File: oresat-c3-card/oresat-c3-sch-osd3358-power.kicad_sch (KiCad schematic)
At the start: 36 parts, among them Q6 MMBT2907, U1 OSD3358-1G-ISM, U10 SN74AUC1G07DCKR, U14 TLVH431

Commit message: Design review on power and RF
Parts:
- U1: Distributor (none) -> DigiKey; MPN OSD3358-1G-ISM -> OSD3358-512M-BSM
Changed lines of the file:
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@@
 			)
 		)
+		(property "Sim.Pins" "1=K 2=A"
+			(at 298.45 82.55 0)
+			(effects
+				(font
+					(size 1.27 1.27)
+				)
+				(hide yes)
+			)
+		)
 		(pin "1"
 		)
@@
 			)
 		)
-		(property "Description" "Embedded Module ARM® Cortex®-A8, AM3358 1GHz 1GB"
+		(property "Description" "OSD335x Embedded Module 1GHz 512MB"
 			(at 224.79 132.08 0)
 			(effects
@@
 			)
 		)
-		(property "MPN" "OSD3358-1G-ISM"
+		(property "MPN" "OSD3358-512M-BSM"
 			(at 224.79 132.08 0)
 			(effects
@@
 			)
 		)
+		(property "Distributor" "DigiKey"
+			(at 224.79 30.48 0)
+			(effects
+				(font
+					(size 1.27 1.27)
+				)
+				(hide yes)
+			)
+		)
 		(pin "C10"
 		)
@@
 			)
 		)
-		(property "Description" "Bipolar (BJT) Transistor PNP 60 V 600 mA 200MHz 250 mW Surface Mount TO-236AB"
+		(property "Description" "PNP transistor, base/emitter/collector"
 			(at 288.29 132.08 0)
 			(effects
@@
 			(at 288.29 132.08 0)
 			(effects
+				(font
+					(size 1.27 1.27)
+				)
+				(hide yes)
+			)
+		)
+		(property "Sim.Device" "PNP"
+			(at 288.29 132.08 0)
+			(effects
+				(font
+					(size 1.27 1.27)
+				)
+				(hide yes)
+			)
+		)
+		(property "Sim.Pins" "1=B 2=E 3=C"
+			(at 288.29 132.08 0)
+			(effects

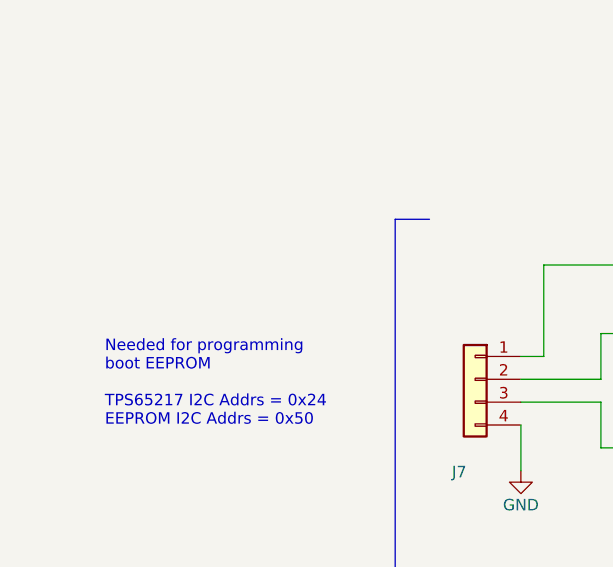
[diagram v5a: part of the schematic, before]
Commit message: Design review on C3 v7.0
Glenn and Andrew did a design review. Removed fiducials on back of board. Lots of schematic fixes, including
direction connection of TCXOs to AT86s, corrected LPF of CLKO from AT86 to the synth reference, fixed drive
levels both QPC switches in UHF radio, confirmed QPC directions, and some minor polishing.
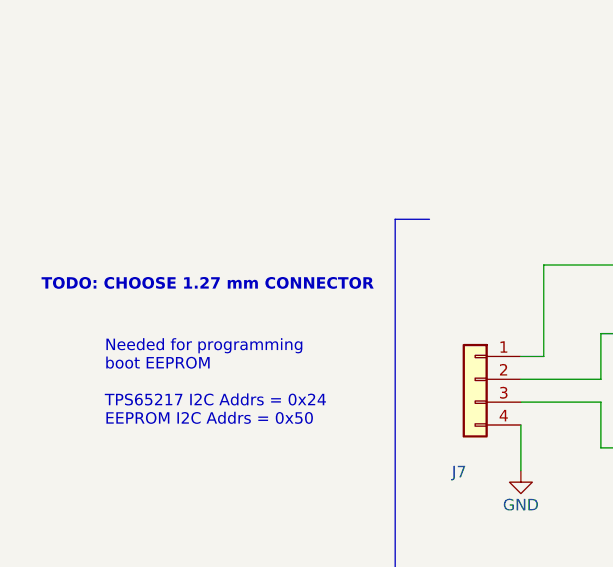
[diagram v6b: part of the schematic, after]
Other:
- note added: "TODO: CHOOSE 1.27 mm CONNECTOR"
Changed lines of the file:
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@@
+		)
+	)
+	(text "TODO: CHOOSE 1.27 mm CONNECTOR"
+		(exclude_from_sim no)
+		(at 130.302 187.706 0)
+		(effects
+			(font
+				(size 1.27 1.27)
+				(thickness 0.254)
+				(bold yes)
+			)
 		)
 	)

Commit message: Updating BOM and switching to oresat-passive footprints. Fixed some power cutoff limits, and fixed another DC voltage leverl on an LNA!
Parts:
- C33, C65, C78, D8, U1, U10, U14: DST Digi-Key -> DigiKey
- Q6: DPN 1727-1884-1-ND -> 1727-2958-1-ND; DST Digi-Key -> DigiKey; MPN PMBT2907A,235 -> PMBT2907A,215
- R50, R53, R54, R57: footprint Resistor_SMD:R_0603_1608Metric -> oresat-passives:0603-C-NOSILK; DST Digi-Key -> DigiKey; MFR Stackpole Electronics Inc -> Stackpole Electronics
- R55, R56: footprint Resistor_SMD:R_0603_1608Metric -> oresat-passives:0603-C-NOSILK; DST Digi-Key -> DigiKey
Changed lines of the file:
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@@
 			)
 		)
-		(property "Datasheet" "~"
+		(property "Datasheet" "https://www.we-online.com/components/products/datasheet/150060GS75000.pdf"
 			(at 298.45 82.55 90)
 			(effects
@@
 			)
 		)
-		(property "Description" "Light emitting diode, small symbol"
+		(property "Description" "Green 520nm LED Indication - Discrete 3.2V 0603 (1608 Metric) - 430 mcd @ 20 mA"
 			(at 298.45 82.55 0)
 			(effects
@@
 			)
 		)
-		(property "DST" "Digi-Key"
+		(property "DST" "DigiKey"
 			(at 298.45 82.55 0)
 			(effects
@@
 			)
 		)
-		(property "Footprint" "Resistor_SMD:R_0603_1608Metric"
+		(property "Footprint" "oresat-passives:0603-C-NOSILK"
 			(at 182.88 218.44 0)
 			(effects
@@
 			)
 		)
-		(property "Datasheet" "~"
+		(property "Datasheet" "https://www.seielect.com/catalog/SEI-RMCF_RMCP.pdf"
 			(at 182.88 218.44 0)
 			(effects
@@
 			)
 		)
-		(property "DST" "Digi-Key"
+		(property "DST" "DigiKey"
 			(at 182.88 218.44 0)
 			(effects
@@
 			)
 		)
-		(property "MFR" "Stackpole Electronics Inc"
+		(property "MFR" "Stackpole Electronics"
 			(at 182.88 218.44 0)
 			(effects
@@
 			)
 		)
-		(property "DST" "Digi-Key"
+		(property "DST" "DigiKey"
 			(at 299.72 219.71 0)
 			(effects
@@
 			)
 		)
-		(property "DST" "Digi-Key"
+		(property "DST" "DigiKey"
 			(at 289.56 190.5 0)
 			(effects
@@
 			)
 		)
-		(property "Footprint" "Resistor_SMD:R_0603_1608Metric"
+		(property "Footprint" "oresat-passives:0603-C-NOSILK"
 			(at 298.45 139.7 0)
 			(effects
@@
 			)
 		)
-		(property "Datasheet" "~"
+		(property "Datasheet" "https://www.seielect.com/catalog/SEI-RMCF_RMCP.pdf"
 			(at 298.45 139.7 0)
 			(effects
@@
 			)
 		)
-		(property "DST" "Digi-Key"
+		(property "DST" "DigiKey"
 			(at 298.45 139.7 0)
 			(effects
@@
 			)
 		)
-		(property "Footprint" "Resistor_SMD:R_0603_1608Metric"
+		(property "Footprint" "oresat-passives:0603-C-NOSILK"
 			(at 308.61 139.7 0)
 			(effects
@@
 			)
 		)
-		(property "Datasheet" "~"
+		(property "Datasheet" "https://www.seielect.com/catalog/SEI-RMCF_RMCP.pdf"
 			(at 308.61 139.7 0)
 			(effects
@@
 			)
 		)
-		(property "DST" "Digi-Key"
+		(property "DST" "DigiKey"
 			(at 308.61 139.7 0)
 			(effects
@@
 			)
 		)
-		(property "MFR" "Stackpole Electronics Inc"
+		(property "MFR" "Stackpole Electronics"
 			(at 308.61 139.7 0)
 			(effects
@@
 			)
 		)
-		(property "DST" "Digi-Key"
+		(property "DST" "DigiKey"
 			(at 177.8 58.42 0)
 			(effects
@@
 			)
 		)
-		(property "Footprint" "Resistor_SMD:R_0603_1608Metric"
+		(property "Footprint" "oresat-passives:0603-C-NOSILK"
 			(at 308.61 114.3 0)
 			(effects
@@
 			)
 		)
-		(property "Datasheet" "~"
+		(property "Datasheet" "https://www.seielect.com/catalog/SEI-RMCF_RMCP.pdf"
 			(at 308.61 114.3 0)
 			(effects
@@
 			)
 		)
-		(property "DST" "Digi-Key"
+		(property "DST" "DigiKey"
 			(at 308.61 114.3 0)
 			(effects
@@
 			)
 		)
-		(property "Datasheet" ""
+		(property "Datasheet" "https://octavosystems.com/docs/osd335x-sm-datasheet/"
 			(at 224.79 132.08 0)
 			(effects
@@
 			)
 		)
-		(property "DST" "Digi-Key"
+		(property "DST" "DigiKey"
 			(at 224.79 132.08 0)
 			(effects
@@
 			)
 		)
-		(property "DST" "Digi-Key"
+		(property "DST" "DigiKey"
 			(at 298.45 124.46 0)
 			(effects
@@
 			)
 		)
-		(property "Datasheet" "~"
+		(property "Datasheet" "https://assets.nexperia.com/documents/data-sheet/PMBT2907A.pdf"
 			(at 288.29 132.08 0)
 			(effects
@@
 			)
 		)
-		(property "Description" "PNP transistor, base/emitter/collector"
+		(property "Description" "Bipolar (BJT) Transistor PNP 60 V 600 mA 200MHz 250 mW Surface Mount TO-236AB"
 			(at 288.29 132.08 0)
 			(effects
@@
 			)
 		)
-		(property "DPN" "1727-1884-1-ND"
+		(property "DPN" "1727-2958-1-ND"
 			(at 288.29 132.08 0)
 			(effects
@@
 			)
 		)
-		(property "DST" "Digi-Key"
+		(property "DST" "DigiKey"
 			(at 288.29 132.08 0)
 			(effects
@@
 			)
 		)
-		(property "MPN" "PMBT2907A,235"
+		(property "MPN" "PMBT2907A,215"
 			(at 288.29 132.08 0)
 			(effects
@@
 			)
 		)
-		(property "Footprint" "Resistor_SMD:R_0603_1608Metric"
+		(property "Footprint" "oresat-passives:0603-C-NOSILK"
 			(at 299.72 210.82 0)
 			(effects
@@
 			)
 		)
-		(property "Datasheet" "~"
+		(property "Datasheet" "https://www.seielect.com/catalog/SEI-RMCF_RMCP.pdf"
 			(at 299.72 210.82 0)
 			(effects
@@
 			)
 		)
-		(property "DST" "Digi-Key"
+		(property "DST" "DigiKey"
 			(at 299.72 210.82 0)
 			(effects
@@
 			)
 		)
-		(property "MFR" "Stackpole Electronics Inc"
+		(property "MFR" "Stackpole Electronics"
 			(at 299.72 210.82 0)
 			(effects
@@
 			)
 		)
-		(property "Footprint" "Resistor_SMD:R_0603_1608Metric"
+		(property "Footprint" "oresat-passives:0603-C-NOSILK"
 			(at 298.45 76.2 0)
 			(effects
@@
 			)
 		)
-		(property "Datasheet" "~"
+		(property "Datasheet" "https://www.seielect.com/catalog/SEI-RMCF_RMCP.pdf"
 			(at 298.45 76.2 0)
 			(effects
@@
 			)
 		)
-		(property "DST" "Digi-Key"
+		(property "DST" "DigiKey"
 			(at 298.45 76.2 0)
 			(effects
@@
 			)
 		)
-		(property "MFR" "Stackpole Electronics Inc"
+		(property "MFR" "Stackpole Electronics"
 			(at 298.45 76.2 0)
 			(effects
@@
 			)
 		)
-		(property "DST" "Digi-Key"
+		(property "DST" "DigiKey"
 			(at 285.75 203.2 0)
 			(effects

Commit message: All footprints updated. Passes ERC/DRC.
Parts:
- C33, C65, C78: footprint Capacitor_SMD:C_0603_1608Metric -> oresat-passives:0603-C-NOSILK; DPN 587-3472-1-ND -> 399-6856-1-ND; MFR Taiyo Yuden -> KEMET; MPN TMK107BJ104KAHT -> C0603C104K5RACAUTO
- C34, C35, C36, C93: DPN 490-GCM32EC71E226KE36KCT-ND -> 587-5949-1-ND; DST Digi-Key -> DigiKey; MFR Murata Electronics -> Taiyo Yuden; MPN GCM32EC71E226KE36K -> TMK325B7226KMHP
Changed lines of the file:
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@@
 			)
 		)
-		(property "Datasheet" "~"
+		(property "Datasheet" "https://mm.digikey.com/Volume0/opasdata/d220001/medias/docus/21/TMK325B7226KMHP_SS.pdf"
 			(at 162.56 58.42 0)
 			(effects
@@
 			)
 		)
-		(property "Description" "22 µF ±10% 25V Ceramic Capacitor X7S 1210 (3225 Metric)"
+		(property "Description" "22 µF ±10% 25V Ceramic Capacitor X7R 1210 (3225 Metric)"
 			(at 162.56 58.42 0)
 			(effects
@@
 			)
 		)
-		(property "DPN" "490-GCM32EC71E226KE36KCT-ND"
+		(property "DPN" "587-5949-1-ND"
 			(at 162.56 58.42 0)
 			(effects
@@
 			)
 		)
-		(property "DST" "Digi-Key"
+		(property "DST" "DigiKey"
 			(at 162.56 58.42 0)
 			(effects
@@
 			)
 		)
-		(property "MFR" "Murata Electronics"
+		(property "MFR" "Taiyo Yuden"
 			(at 162.56 58.42 0)
 			(effects
@@
 			)
 		)
-		(property "MPN" "GCM32EC71E226KE36K"
+		(property "MPN" "TMK325B7226KMHP"
 			(at 162.56 58.42 0)
 			(effects
@@
 			)
 		)
-		(property "Footprint" "Capacitor_SMD:C_0603_1608Metric"
+		(property "Footprint" "oresat-passives:0603-C-NOSILK"
 			(at 299.72 219.71 0)
 			(effects
@@
 			)
 		)
-		(property "Datasheet" "~"
+		(property "Datasheet" "https://search.kemet.com/download/specsheet/C0603C104K5RACAUTO"
 			(at 299.72 219.71 0)
 			(effects
@@
 			)
 		)
-		(property "Description" "100 nF (0.1µF) ±10% 25V Ceramic Capacitor X5R 0603 (1608 Metric)"
+		(property "Description" "0.1 µF ±10% 50V Ceramic Capacitor X7R 0603 (1608 Metric)"
 			(at 299.72 219.71 0)
 			(effects
@@
 			)
 		)
-		(property "DPN" "587-3472-1-ND"
+		(property "DPN" "399-6856-1-ND"
 			(at 299.72 219.71 0)
 			(effects
@@
 			)
 		)
-		(property "MFR" "Taiyo Yuden"
+		(property "MFR" "KEMET"
 			(at 299.72 219.71 0)
 			(effects
@@
 			)
 		)
-		(property "MPN" "TMK107BJ104KAHT"
+		(property "MPN" "C0603C104K5RACAUTO"
 			(at 299.72 219.71 0)
 			(effects
@@
 			)
 		)
-		(property "Footprint" "Capacitor_SMD:C_0603_1608Metric"
+		(property "Footprint" "oresat-passives:0603-C-NOSILK"
 			(at 289.56 190.5 0)
 			(effects
@@
 			)
 		)
-		(property "Datasheet" "~"
+		(property "Datasheet" "https://search.kemet.com/download/specsheet/C0603C104K5RACAUTO"
 			(at 289.56 190.5 0)
 			(effects
@@
 			)
 		)
-		(property "Description" "100 nF (0.1µF) ±10% 25V Ceramic Capacitor X5R 0603 (1608 Metric)"
+		(property "Description" "0.1 µF ±10% 50V Ceramic Capacitor X7R 0603 (1608 Metric)"
 			(at 289.56 190.5 0)
 			(effects
@@
 			)
 		)
-		(property "DPN" "587-3472-1-ND"
+		(property "DPN" "399-6856-1-ND"
 			(at 289.56 190.5 0)
 			(effects
@@
 			)
 		)
-		(property "MFR" "Taiyo Yuden"
+		(property "MFR" "KEMET"
 			(at 289.56 190.5 0)
 			(effects
@@
 			)
 		)
-		(property "MPN" "TMK107BJ104KAHT"
+		(property "MPN" "C0603C104K5RACAUTO"
 			(at 289.56 190.5 0)
 			(effects
@@
 			)
 		)
-		(property "Footprint" "Capacitor_SMD:C_0603_1608Metric"
+		(property "Footprint" "oresat-passives:0603-C-NOSILK"
 			(at 177.8 58.42 0)
 			(effects
@@
 			)
 		)
-		(property "Datasheet" "~"
+		(property "Datasheet" "https://search.kemet.com/download/specsheet/C0603C104K5RACAUTO"
 			(at 177.8 58.42 0)
 			(effects
@@
 			)
 		)
-		(property "Description" "100 nF (0.1µF) ±10% 25V Ceramic Capacitor X5R 0603 (1608 Metric)"
+		(property "Description" "0.1 µF ±10% 50V Ceramic Capacitor X7R 0603 (1608 Metric)"
 			(at 177.8 58.42 0)
 			(effects
@@
 			)
 		)
-		(property "DPN" "587-3472-1-ND"
+		(property "DPN" "399-6856-1-ND"
 			(at 177.8 58.42 0)
 			(effects
@@
 			)
 		)
-		(property "MFR" "Taiyo Yuden"
+		(property "MFR" "KEMET"
 			(at 177.8 58.42 0)
 			(effects
@@
 			)
 		)
-		(property "MPN" "TMK107BJ104KAHT"
+		(property "MPN" "C0603C104K5RACAUTO"
 			(at 177.8 58.42 0)
 			(effects
@@
 			)
 		)
-		(property "Datasheet" "~"
+		(property "Datasheet" "https://mm.digikey.com/Volume0/opasdata/d220001/medias/docus/21/TMK325B7226KMHP_SS.pdf"
 			(at 285.75 58.42 0)
 			(effects
@@
 			)
 		)
-		(property "Description" "22 µF ±10% 25V Ceramic Capacitor X7S 1210 (3225 Metric)"
+		(property "Description" "22 µF ±10% 25V Ceramic Capacitor X7R 1210 (3225 Metric)"
 			(at 285.75 58.42 0)
 			(effects
@@
 			)
 		)
-		(property "DPN" "490-GCM32EC71E226KE36KCT-ND"
+		(property "DPN" "587-5949-1-ND"
 			(at 285.75 58.42 0)
 			(effects
@@
 			)
 		)
-		(property "DST" "Digi-Key"
+		(property "DST" "DigiKey"
 			(at 285.75 58.42 0)
 			(effects
@@
 			)
 		)
-		(property "MFR" "Murata Electronics"
+		(property "MFR" "Taiyo Yuden"
 			(at 285.75 58.42 0)
 			(effects
@@
 			)
 		)
-		(property "MPN" "GCM32EC71E226KE36K"
+		(property "MPN" "TMK325B7226KMHP"
 			(at 285.75 58.42 0)
 			(effects
@@
 			)
 		)
-		(property "Datasheet" "~"
+		(property "Datasheet" "https://mm.digikey.com/Volume0/opasdata/d220001/medias/docus/21/TMK325B7226KMHP_SS.pdf"
 			(at 166.37 58.42 0)
 			(effects
@@
 			)
 		)
-		(property "Description" "22 µF ±10% 25V Ceramic Capacitor X7S 1210 (3225 Metric)"
+		(property "Description" "22 µF ±10% 25V Ceramic Capacitor X7R 1210 (3225 Metric)"
 			(at 166.37 58.42 0)
 			(effects
@@
 			)
 		)
-		(property "DPN" "490-GCM32EC71E226KE36KCT-ND"
+		(property "DPN" "587-5949-1-ND"
 			(at 166.37 58.42 0)
 			(effects
@@
 			)
 		)
-		(property "DST" "Digi-Key"
+		(property "DST" "DigiKey"
 			(at 166.37 58.42 0)
 			(effects
@@
 			)
 		)
-		(property "MFR" "Murata Electronics"
+		(property "MFR" "Taiyo Yuden"
 			(at 166.37 58.42 0)
 			(effects
@@
 			)
 		)
-		(property "MPN" "GCM32EC71E226KE36K"
+		(property "MPN" "TMK325B7226KMHP"
 			(at 166.37 58.42 0)
 			(effects
@@
 			)
 		)
-		(property "Datasheet" "~"
+		(property "Datasheet" "https://mm.digikey.com/Volume0/opasdata/d220001/medias/docus/21/TMK325B7226KMHP_SS.pdf"
 			(at 166.37 76.2 0)
 			(effects
@@
 			)
 		)
-		(property "Description" "22 µF ±10% 25V Ceramic Capacitor X7S 1210 (3225 Metric)"
+		(property "Description" "22 µF ±10% 25V Ceramic Capacitor X7R 1210 (3225 Metric)"
 			(at 166.37 76.2 0)
 			(effects
@@
 			)
 		)
-		(property "DPN" "490-GCM32EC71E226KE36KCT-ND"
+		(property "DPN" "587-5949-1-ND"
 			(at 166.37 76.2 0)
 			(effects
@@
 			)
 		)
-		(property "DST" "Digi-Key"
+		(property "DST" "DigiKey"
 			(at 166.37 76.2 0)
 			(effects
@@
 			)
 		)
-		(property "MFR" "Murata Electronics"
+		(property "MFR" "Taiyo Yuden"
 			(at 166.37 76.2 0)
 			(effects
@@
 			)
 		)
-		(property "MPN" "GCM32EC71E226KE36K"
+		(property "MPN" "TMK325B7226KMHP"
 			(at 166.37 76.2 0)
 			(effects
